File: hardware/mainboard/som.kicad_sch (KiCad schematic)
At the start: 15 parts, among them SW1 SW_DIP_x04, U1 CP3225-100.000-3.3-25-X-T-TR, U2 AX3HAF1-135.0000T

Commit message: Misc tweaks
Signed-off-by: gatecat <gatecat@ds0.me>
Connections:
- net +3V3PL: now also U2.1 (E/D)
- no-connect marks 129 -> 128
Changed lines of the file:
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@@
   (no_connect (at 153.67 63.5))
   (no_connect (at 153.67 40.64))
-  (no_connect (at 430.53 151.13))
   (no_connect (at 77.47 129.54))
   (no_connect (at 306.07 137.16))
@@
     (stroke (width 0) (type default))
   )
+  (wire (pts (xy 420.37 151.13) (xy 430.53 151.13))
+    (stroke (width 0) (type default))
+  )
   (wire (pts (xy 224.79 30.48) (xy 229.87 30.48))
     (stroke (width 0) (type default))
@@
     (stroke (width 0) (type default))
   )
+  (wire (pts (xy 420.37 147.32) (xy 420.37 151.13))
+    (stroke (width 0) (type default))
+  )
   (wire (pts (xy 74.93 137.16) (xy 77.47 137.16))
     (stroke (width 0) (type default))
@@
         )
       )
+    )
+  )
+  (symbol (lib_id "meowality:+3V3PL") (at 420.37 147.32 0) (unit 1)
+    (in_bom yes) (on_board yes) (dnp no) (fields_autoplaced)
+    (property "Reference" "#PWR016" (at 420.37 151.13 0)
+      (effects (font (size 1.27 1.27)) hide)
+    )
+    (property "Value" "+3V3PL" (at 420.37 142.24 0)
+      (effects (font (size 1.27 1.27)))
+    )
+    (property "Footprint" "" (at 420.37 147.32 0)
+      (effects (font (size 1.27 1.27)) hide)
+    )
+    (property "Datasheet" "" (at 420.37 147.32 0)
+      (effects (font (size 1.27 1.27)) hide)
+    )
+    (pin "1")
+    (instances
+      (project "meowality-main"
+        (path "/e63e39d7-6ac0-4ffd-8aa3-1841a4541b55/a559f63f-b3a0-4b81-aa6a-605d4da47af6"
+          (reference "#PWR016") (unit 1)
+        )
+      )

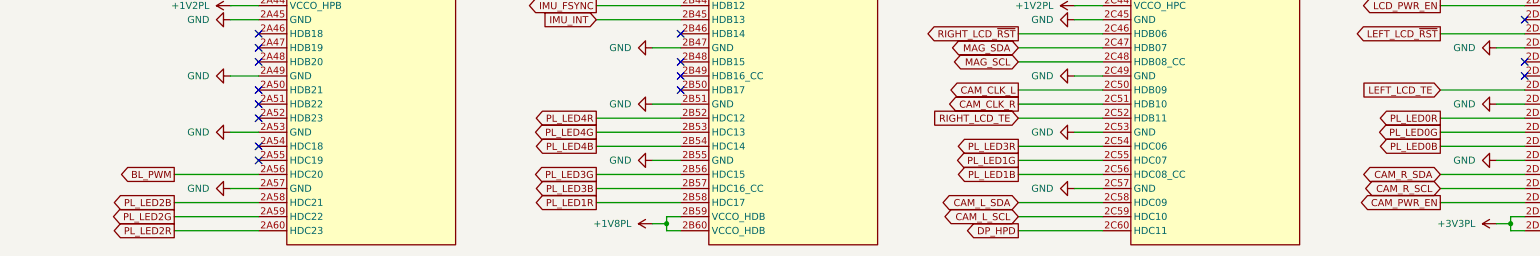
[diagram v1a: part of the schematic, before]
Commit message: hardware: LED associated DFM improvement
Signed-off-by: gatecat <gatecat@ds0.me>
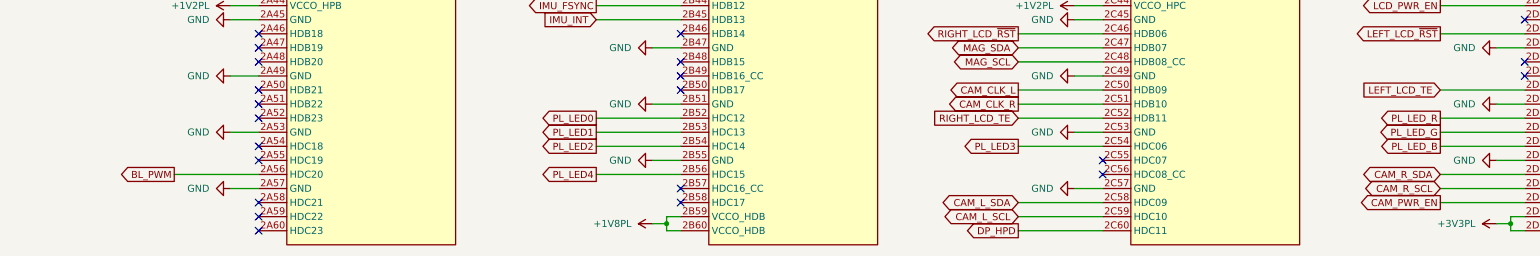
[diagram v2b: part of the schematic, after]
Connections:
- net PL_LED0B renamed PL_LED_B
- net PL_LED0G renamed PL_LED_G
- net PL_LED0R renamed PL_LED_R
- net PL_LED1B: no longer names the net of SOM1.2C56 (HDC08_CC)
- net PL_LED1G: no longer names the net of SOM1.2C55 (HDC07)
- net PL_LED1R: no longer names the net of SOM1.2B58 (HDC17)
- net PL_LED2B: no longer names the net of SOM1.2A58 (HDC21)
- net PL_LED2G: no longer names the net of SOM1.2A59 (HDC22)
- net PL_LED2R: no longer names the net of SOM1.2A60 (HDC23)
- net PL_LED3B: no longer names the net of SOM1.2B57 (HDC16_CC)
- net PL_LED3G renamed PL_LED4
- net PL_LED3R renamed PL_LED3
- net PL_LED4B renamed PL_LED2
- net PL_LED4G renamed PL_LED1
- net PL_LED4R renamed PL_LED0
- no-connect marks 128 -> 135
